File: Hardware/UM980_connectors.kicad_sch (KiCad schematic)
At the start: 6 parts, among them J2 Conn_01x12, J4 Qwiic_RA, J6 JST_Locking_4, J7 Qwiic_RA, J8 Conn_01x09

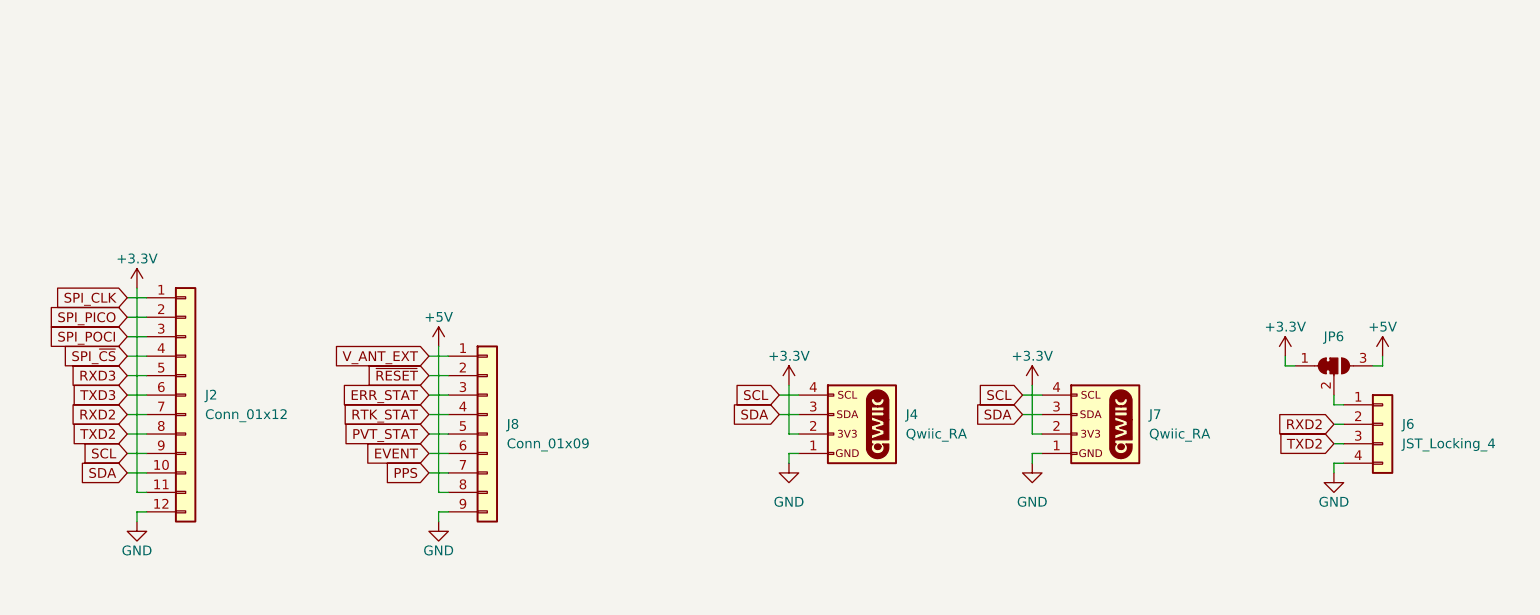
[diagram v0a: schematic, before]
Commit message: Update design with PROD_IDs
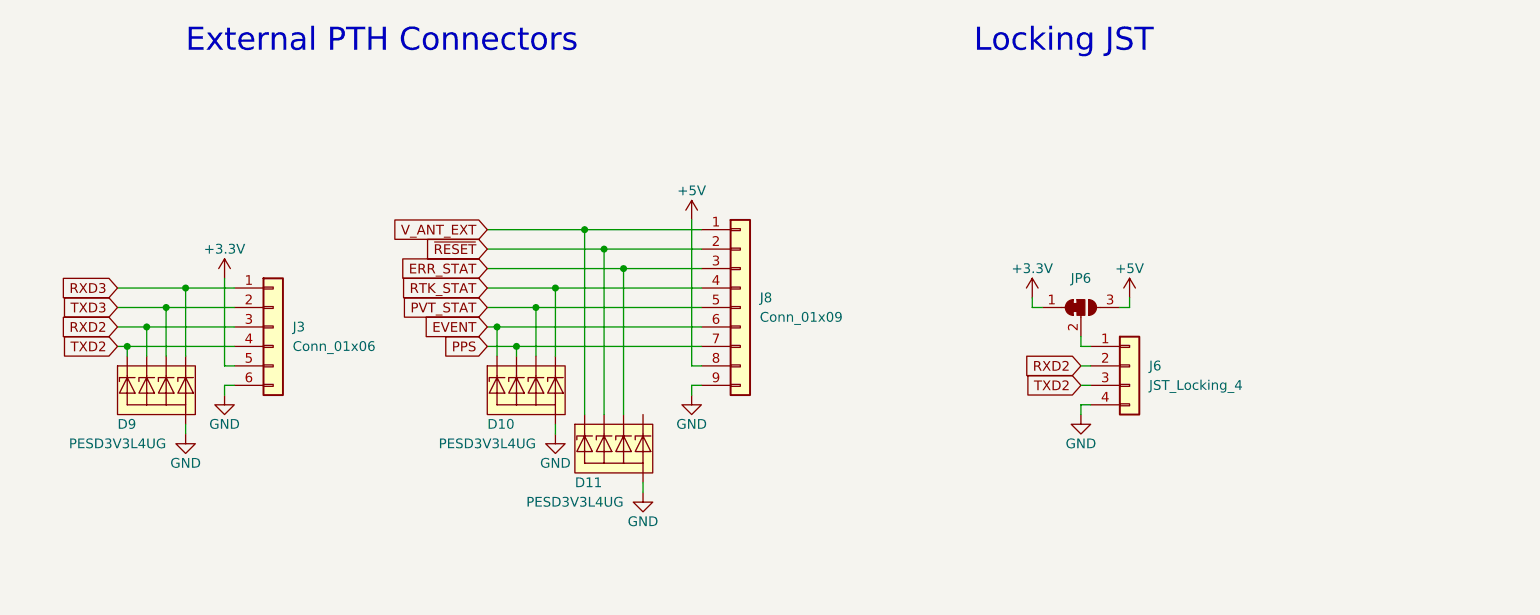
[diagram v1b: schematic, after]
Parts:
- removed J2: Conn_01x12, SparkFun-Connector:1X12, symbol SparkFun-Connector:Conn_01x12
- removed J4, J7: Qwiic_RA, SparkFun-Connector:JST04_1MM_RA, symbol SparkFun-Connector:Qwiic_Right_Angle
- added D10, D11, D9: PESD3V3L4UG, SparkFun-Semiconductor-Standard:SOT-353, symbol SparkFun-DiscreteSemi:PESD3V3L4UG
- added J3: Conn_01x06, SparkFun-Connector:1X06, symbol SparkFun-Connector:Conn_01x06
- J6: PROD_ID (none) -> CONN-15303
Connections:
- net +3.3V: now also J3.5 (Pin_5)
- net ERR_STAT: now also D11.4 (K3)
- net EVENT: now also D10.1 (K1)
- net GND: now also D10.2 (A), D11.2 (A), D9.2 (A), J3.6 (Pin_6)
- net PPS: now also D10.3 (K2)
- net PVT_STAT: now also D10.4 (K3)
- net RTK_STAT: now also D10.5 (K4)
- net RXD2: now also D9.3 (K2), J3.3 (Pin_3)
- net RXD3: now also D9.5 (K4), J3.1 (Pin_1)
- net TXD2: now also D9.1 (K1), J3.4 (Pin_4)
- net TXD3: now also D9.4 (K3), J3.2 (Pin_2)
- net V_ANT_EXT: now also D11.1 (K1)
- net ~{RESET}: now also D11.3 (K2)
- new net: J6.NC1 (NC), J6.NC2 (NC)
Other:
- note added: "External PTH Connectors"
- note added: "Locking JST"
- moved on the sheet: J6, J8, JP6

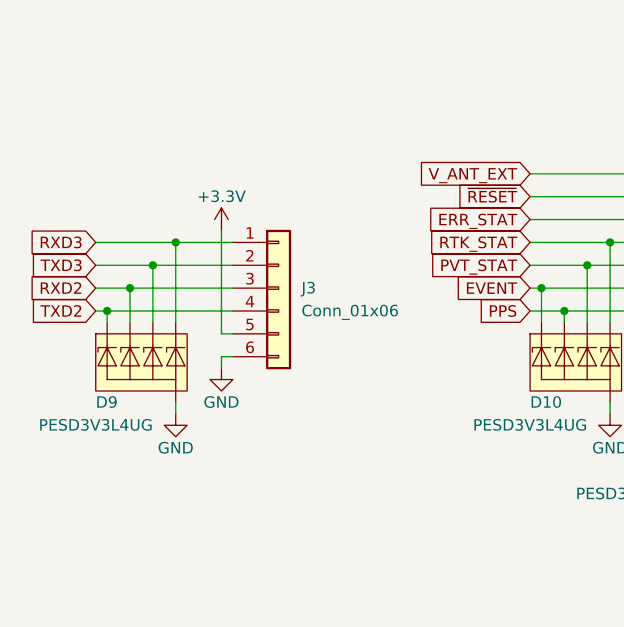
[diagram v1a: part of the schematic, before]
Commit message: Change port 3 to be compatible with BlueSMiRF
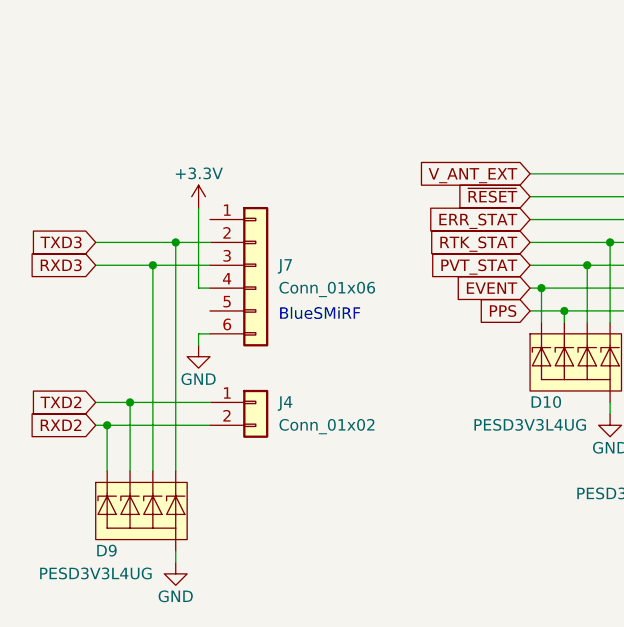
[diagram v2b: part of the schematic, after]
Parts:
- removed J3: Conn_01x06, SparkFun-Connector:1X06, symbol SparkFun-Connector:Conn_01x06
- added J4: Conn_01x02, SparkFun-Connector:1X02, symbol SparkFun-Connector:Conn_01x02
- added J7: Conn_01x06, SparkFun-Connector:1X06, symbol SparkFun-Connector:Conn_01x06
- D10, D11, D9: symbol SparkFun-DiscreteSemi:PESD3V3L4UG -> SparkFun-DiscreteSemi:D_TVS_ESD_4
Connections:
- net +3.3V: now also J7.4 (Pin_4)
- net GND: now also J7.6 (Pin_6)
- net RXD2: now also D9.1 (K1), J4.2 (Pin_2); no longer D9.3 (K2)
- net RXD3: now also D9.4 (K3), J7.3 (Pin_3); no longer D9.5 (K4)
- net TXD2: now also D9.3 (K2), J4.1 (Pin_1); no longer D9.1 (K1)
- net TXD3: now also D9.5 (K4), J7.2 (Pin_2); no longer D9.4 (K3)
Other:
- note added: "BlueSMiRF"
- moved on the sheet: D9

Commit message: Post design review.
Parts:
- added JP8: BT-VCC, SparkFun-Jumper:SMT-JUMPER_2_NC_TRACE_SILK, symbol SparkFun-Jumper:SolderJumper_2_Bridged
- added R8: 1k, SparkFun-Resistor:R_0603_1608Metric, symbol SparkFun-Resistor:1k_0603
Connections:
- net +3.3V: now also JP8.2 (B); no longer J7.4 (Pin_4)
- net RXD2: now also R8.1; no longer J6.2 (Pin_2)
- new net: J7.4 (Pin_4), JP8.1 (A)
- new net: J6.2 (Pin_2), R8.2

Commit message: Update to v8. Update models.
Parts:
- J4: footprint SparkFun-Connector:1X02 -> SparkFun-Connector:1x02
- J6: footprint SparkFun-Connector:JST-4-SMD-1.25MM-LOCKING -> SparkFun-Connector:JST_SMD_1.25mm-4_Locking
- J7: footprint SparkFun-Connector:1X06 -> SparkFun-Connector:1x06
- J8: footprint SparkFun-Connector:1X09 -> SparkFun-Connector:1x09
- JP6: footprint SparkFun-Jumper:SMT-JUMPER_3_1-NC_TRACE_SILK -> SparkFun-Jumper:Jumper_3_NC-1_Trace
- JP8: value BT-VCC -> ~; footprint SparkFun-Jumper:SMT-JUMPER_2_NC_TRACE_SILK -> SparkFun-Jumper:Jumper_2_NC_Trace
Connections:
- net +3.3V renamed 3.3V
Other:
- moved on the sheet: R8
